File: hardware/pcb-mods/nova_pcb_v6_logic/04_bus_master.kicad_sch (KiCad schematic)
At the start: 4 parts, among them J9 FE-URT-1, U6 Teensy4.1, U7 74HC125

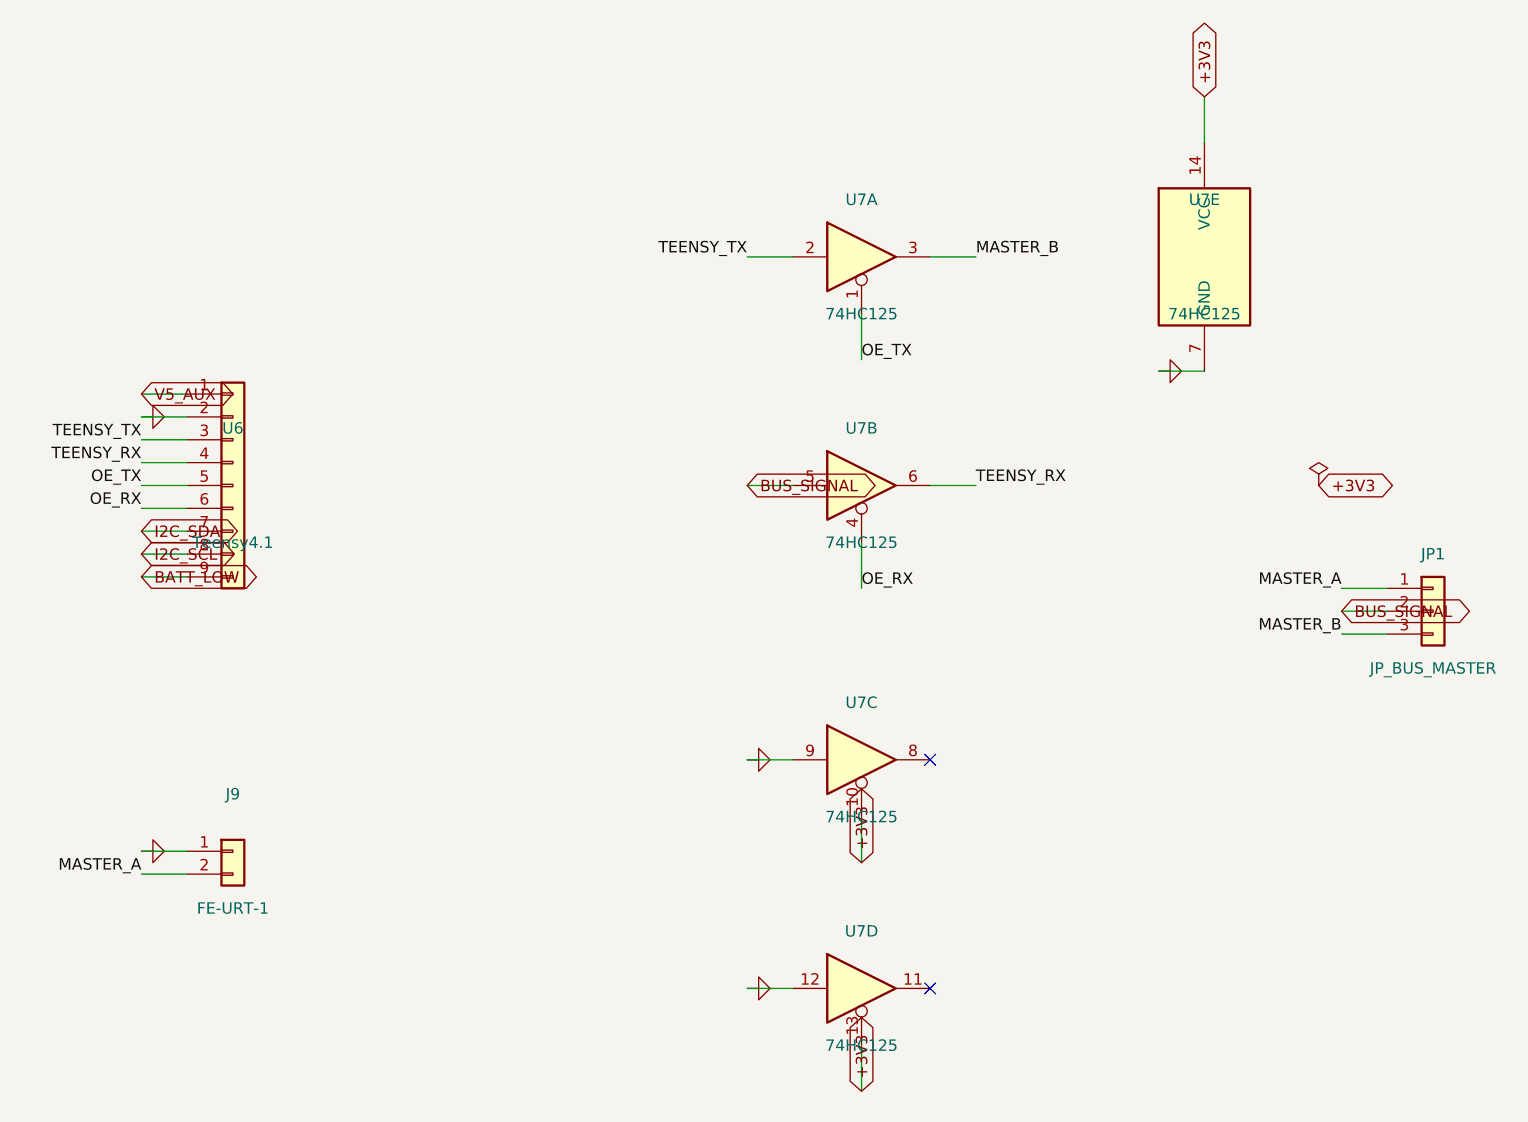
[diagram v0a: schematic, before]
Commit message: fix(logic): +3V3 sourced from Teensy 3.3V (T3V3O pin added) — board-killer bug fixed
Netlist verified: +3V3 = [U6.T3V3O(3V3), U7.10/13/14(VCC), J20.5]. 74HC125
+ 3x INA226 now powered. Combined with R1/FB1 un-DNP, both logic-board
bugs from the 2026-06-13 review are resolved. Board left unrouted-clean
for autorouting (Freerouting).

Co-Authored-By: Claude Fable 5 <noreply@anthropic.com>
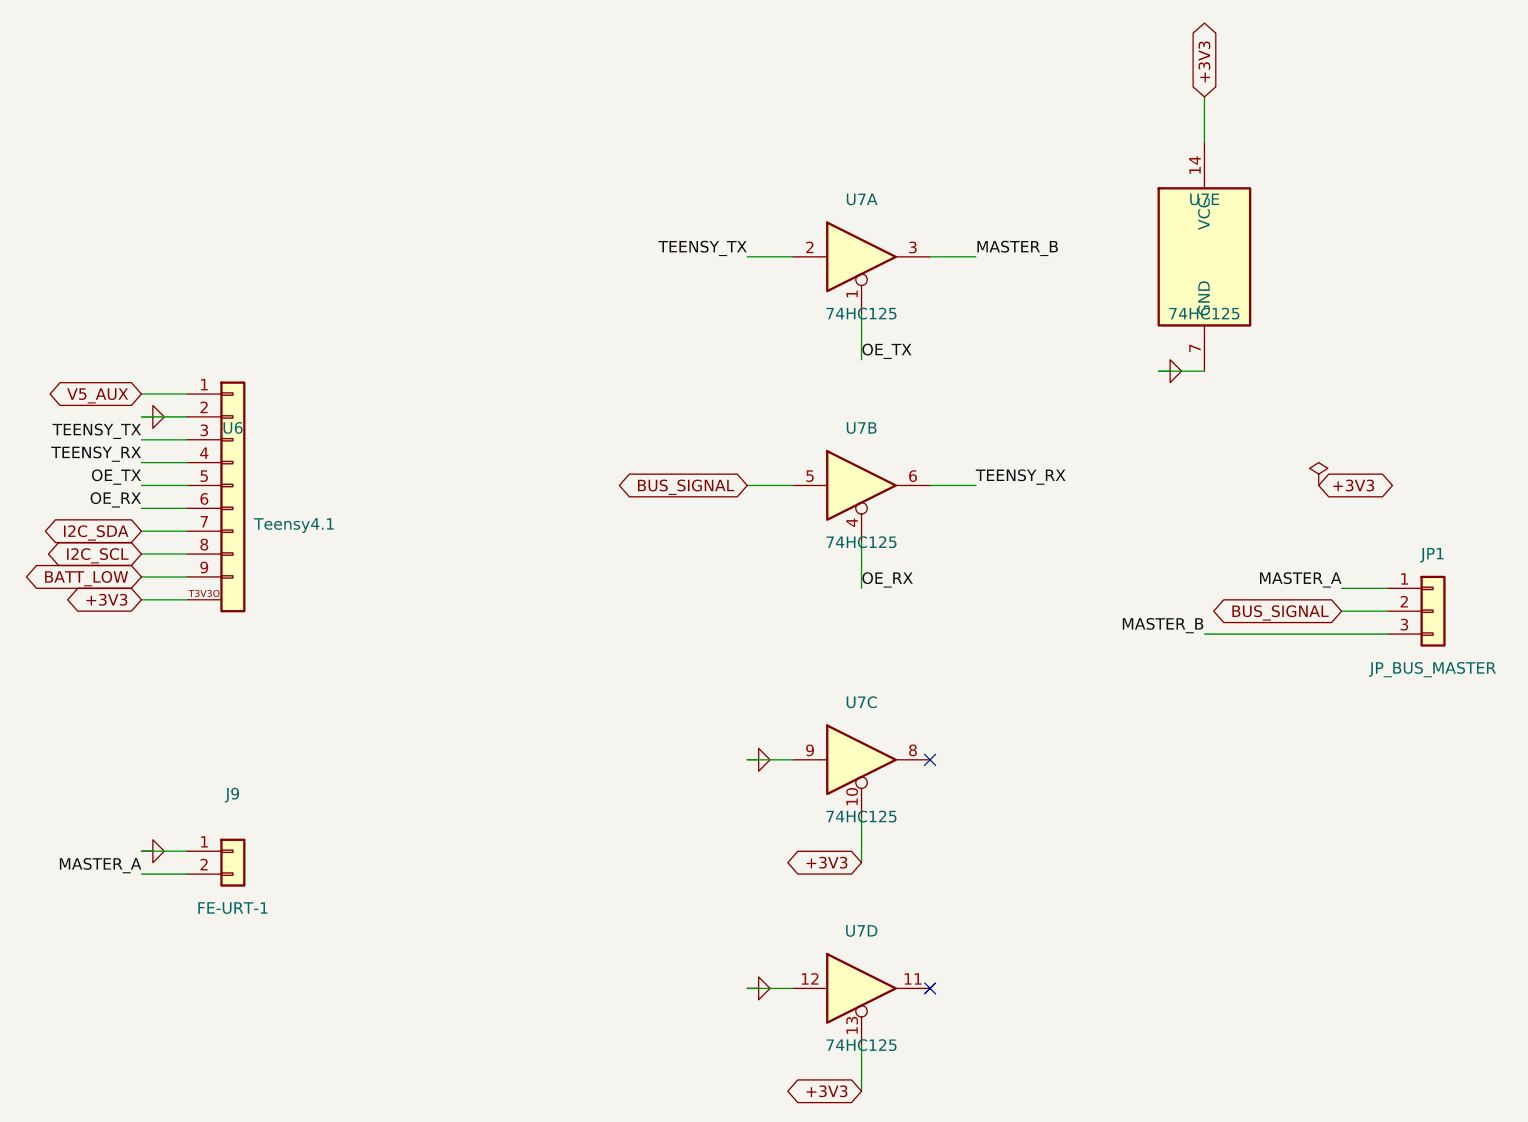
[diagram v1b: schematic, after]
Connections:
- net +3V3: now also U6.T3V3O (3V3)
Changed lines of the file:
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@@
 	(wire
 		(pts
-			(xy 39.37 81.28) (xy 34.29 81.28)
+			(xy 34.29 88.9) (xy 39.37 88.9)
 		)
 		(stroke
@@
 	(wire
 		(pts
+			(xy 34.29 81.28) (xy 39.37 81.28)
+		)
+		(stroke
+			(width 0)
+			(type default)
+		)
+	)
+	(wire
+		(pts
+			(xy 34.29 71.12) (xy 39.37 71.12)
+		)
+		(stroke
+			(width 0)
+			(type default)
+		)
+	)
+	(wire
+		(pts
 			(xy 152.4 63.5) (xy 147.32 63.5)
 		)
@@
 	(wire
 		(pts
-			(xy 39.37 71.12) (xy 34.29 71.12)
-		)
-		(stroke
-			(width 0)
-			(type default)
-		)
-	)
-	(wire
-		(pts
 			(xy 114.3 57.15) (xy 114.3 62.23)
 		)
@@
 	(wire
 		(pts
-			(xy 172.72 92.71) (xy 167.64 92.71)
+			(xy 172.72 92.71) (xy 152.4 92.71)
 		)
 		(stroke
@@
 	)
 	(label "MASTER_B"
-		(at 167.64 92.71 180)
+		(at 152.4 92.71 180)
 		(effects
 			(font
@@
 	(global_label "I2C_SCL"
 		(shape bidirectional)
-		(at 34.29 83.82 0)
+		(at 34.29 83.82 180)
+		(effects
+			(font
+				(size 1.27 1.27)
+			)
+			(justify right)
+		)
+		(property "Intersheetrefs" "${INTERSHEET_REFS}"
+			(at 34.29 83.82 0)
+			(effects
+				(font
+					(size 1.27 1.27)
+				)
+				(hide yes)
+			)
+		)
+	)
+	(global_label "BUS_SIGNAL"
+		(shape bidirectional)
+		(at 167.64 90.17 180)
+		(effects
+			(font
+				(size 1.27 1.27)
+			)
+			(justify right)
+		)
+		(property "Intersheetrefs" "${INTERSHEET_REFS}"
+			(at 167.64 90.17 0)
+			(effects
+				(font
+					(size 1.27 1.27)
+				)
+				(hide yes)
+			)
+		)
+	)
+	(global_label "+3V3"
+		(shape bidirectional)
+		(at 34.29 88.9 180)
+		(effects
+			(font
+				(size 1.27 1.27)
+			)
+			(justify right)
+		)
+		(property "Intersheetrefs" "${INTERSHEET_REFS}"
+			(at 34.29 88.9 90)
+			(effects
+				(font
+					(size 1.27 1.27)
+				)
+				(hide yes)
+			)
+		)
+	)
+	(global_label "+3V3"
+		(shape bidirectional)
+		(at 165.1 76.2 0)
 		(effects
 			(font
@@
 		)
 		(property "Intersheetrefs" "${INTERSHEET_REFS}"
-			(at 34.29 83.82 0)
+			(at 165.1 76.2 0)
 			(effects
 				(font
@@
 	(global_label "BUS_SIGNAL"
 		(shape bidirectional)
-		(at 167.64 90.17 0)
-		(effects
-			(font
-				(size 1.27 1.27)
-			)
-			(justify left)
-		)
-		(property "Intersheetrefs" "${INTERSHEET_REFS}"
-			(at 167.64 90.17 0)
+		(at 101.6 76.2 180)
+		(effects
+			(font
+				(size 1.27 1.27)
+			)
+			(justify right)
+		)
+		(property "Intersheetrefs" "${INTERSHEET_REFS}"
+			(at 101.6 76.2 0)
 			(effects
 				(font
@@
 	(global_label "+3V3"
 		(shape bidirectional)
-		(at 165.1 76.2 0)
-		(effects
-			(font
-				(size 1.27 1.27)
-			)
-			(justify left)
-		)
-		(property "Intersheetrefs" "${INTERSHEET_REFS}"
-			(at 165.1 76.2 0)
-			(effects
-				(font
-					(size 1.27 1.27)
-				)
-				(hide yes)
-			)
-		)
-	)
-	(global_label "BUS_SIGNAL"
-		(shape bidirectional)
-		(at 101.6 76.2 0)
-		(effects
-			(font
-				(size 1.27 1.27)
-			)
-			(justify left)
-		)
-		(property "Intersheetrefs" "${INTERSHEET_REFS}"
-			(at 101.6 76.2 0)
+		(at 114.3 118.11 180)
+		(effects
+			(font
+				(size 1.27 1.27)
+			)
+			(justify right)
+		)
+		(property "Intersheetrefs" "${INTERSHEET_REFS}"
+			(at 114.3 118.11 90)
+			(effects
+				(font
+					(size 1.27 1.27)
+				)
+				(hide yes)
+			)
+		)
+	)
+	(global_label "BATT_LOW"
+		(shape bidirectional)
+		(at 34.29 86.36 180)
+		(effects
+			(font
+				(size 1.27 1.27)
+			)
+			(justify right)
+		)
+		(property "Intersheetrefs" "${INTERSHEET_REFS}"
+			(at 34.29 86.36 0)
+			(effects
+				(font
+					(size 1.27 1.27)
+				)
+				(hide yes)
+			)
+		)
+	)
+	(global_label "V5_AUX"
+		(shape bidirectional)
+		(at 34.29 66.04 180)
+		(effects
+			(font
+				(size 1.27 1.27)
+			)
+			(justify right)
+		)
+		(property "Intersheetrefs" "${INTERSHEET_REFS}"
+			(at 34.29 66.04 0)
 			(effects
 				(font
@@
 	(global_label "+3V3"
 		(shape bidirectional)
-		(at 114.3 118.11 90)
-		(effects
-			(font
-				(size 1.27 1.27)
-			)
-			(justify left)
-		)
-		(property "Intersheetrefs" "${INTERSHEET_REFS}"
-			(at 114.3 118.11 0)
-			(effects
-				(font
-					(size 1.27 1.27)
-				)
-				(hide yes)
-			)
-		)
-	)
-	(global_label "BATT_LOW"
-		(shape bidirectional)
-		(at 34.29 86.36 0)
-		(effects
-			(font
-				(size 1.27 1.27)
-			)
-			(justify left)
-		)
-		(property "Intersheetrefs" "${INTERSHEET_REFS}"
-			(at 34.29 86.36 0)
-			(effects
-				(font
-					(size 1.27 1.27)
-				)
-				(hide yes)
-			)
-		)
-	)
-	(global_label "V5_AUX"
-		(shape bidirectional)
-		(at 34.29 66.04 0)
-		(effects
-			(font
-				(size 1.27 1.27)
-			)
-			(justify left)
-		)
-		(property "Intersheetrefs" "${INTERSHEET_REFS}"
-			(at 34.29 66.04 0)
-			(effects
-				(font
-					(size 1.27 1.27)
-				)
-				(hide yes)
-			)
-		)
-	)
-	(global_label "+3V3"
-		(shape bidirectional)
-		(at 114.3 143.51 90)
-		(effects
-			(font
-				(size 1.27 1.27)
-			)
-			(justify left)
-		)
-		(property "Intersheetrefs" "${INTERSHEET_REFS}"
-			(at 114.3 143.51 0)
+		(at 114.3 143.51 180)
+		(effects
+			(font
+				(size 1.27 1.27)
+			)
+			(justify right)
+		)
+		(property "Intersheetrefs" "${INTERSHEET_REFS}"
+			(at 114.3 143.51 90)
 			(effects
 				(font
@@
 	(global_label "I2C_SDA"
 		(shape bidirectional)
-		(at 34.29 81.28 0)
-		(effects
-			(font
-				(size 1.27 1.27)
-			)
-			(justify left)
+		(at 34.29 81.28 180)
+		(effects
+			(font
+				(size 1.27 1.27)
+			)
+			(justify right)
 		)
 		(property "Intersheetrefs" "${INTERSHEET_REFS}"
@@
 		)
 		(property "Value" "Teensy4.1"
-			(at 44.45 82.55 0)
+			(at 51.308 80.518 0)
 			(effects
 				(font
@@
 		(pin "9"
 		)
+		(pin "T3V3O"
+		)
 		(instances

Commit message: pcb(logic): add C1 100nF decoupling at U7 + re-route — DRC 0/0 COMPLETE
C1 (CC0603 100nF) across +3V3/GND placed next to U7 pin14; full board
re-routed via Freerouting (25 nets, 159 tracks, 2 vias). DRC: 0 errors,
0 unconnected. 7 cosmetic lib warnings. Logic board fab-ready.

Co-Authored-By: Claude Fable 5 <noreply@anthropic.com>
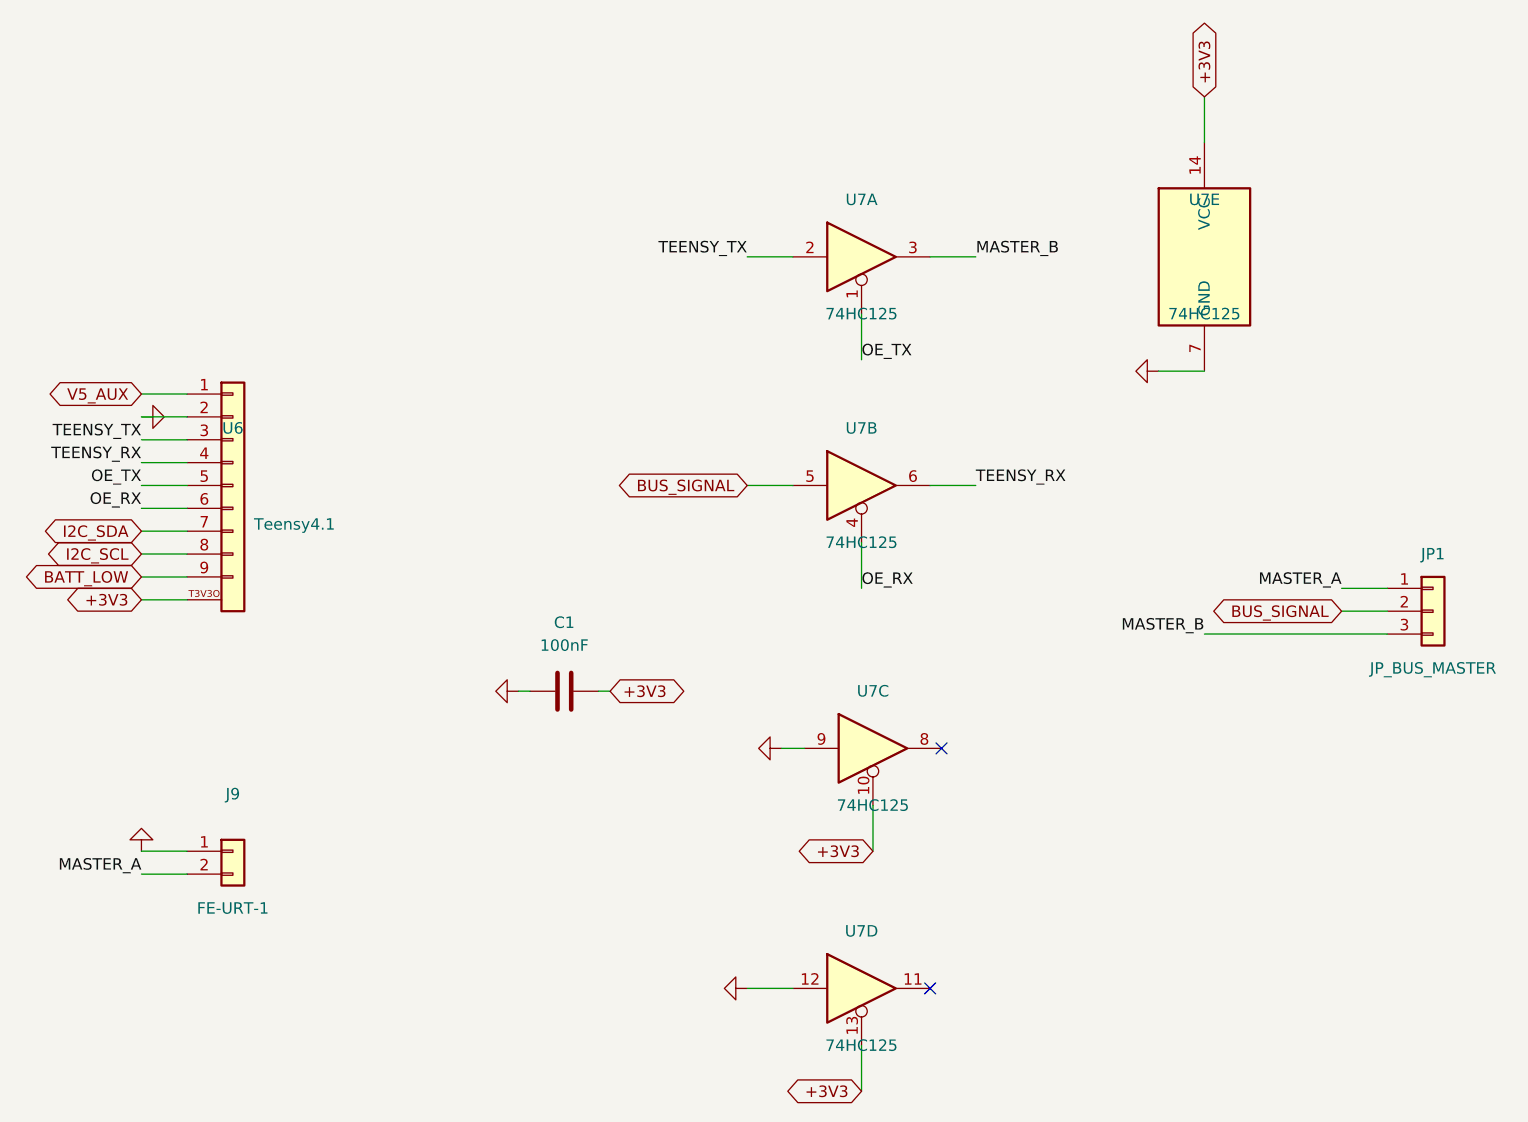
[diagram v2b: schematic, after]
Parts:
- added C1: 100nF, Capacitor_SMD:C_0603_1608Metric, symbol Device:C
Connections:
- net +3V3: now also C1.2
- net GND: now also C1.1
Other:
- moved on the sheet: U7C
